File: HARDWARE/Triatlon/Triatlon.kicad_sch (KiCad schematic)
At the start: 18 parts, among them J1 TCRT5000-1, J2 TCRT5000-2, J3 Conn_01x10, J4 TCRT5000-3, J5 TB_1X2, SW1 SW1, U1 ESP32_DEVKITC, U2 Mini360, U3 AMS1117-3.3

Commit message: Prueba
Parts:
- added D1: 1N4148WT, Diode_SMD:D_SOD-523, symbol Diode:1N4148WT
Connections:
- net GND: now also U1.32 (GND), U1.38 (GND)
- net LPWM1: now also U1.23 (IO15)
- net LPWM2: now also U1.36 (IO22)
- net RPWM1: now also U1.26 (IO4)
- net RPWM2: now also U1.37 (IO23)
- net VCC: no longer J5.1
- new net: D1.1 (K), D1.2 (A)
- new net 7.4V: J5.1
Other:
- moved on the sheet: U1

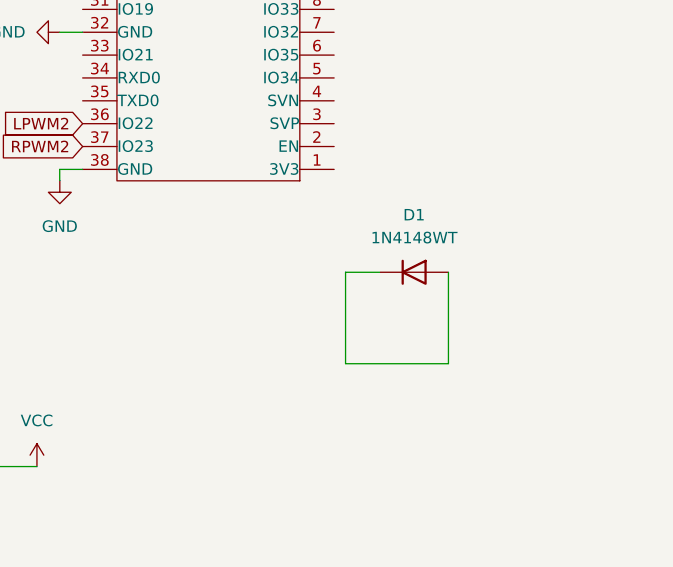
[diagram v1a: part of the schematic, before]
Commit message: Reestablezco el esquematico
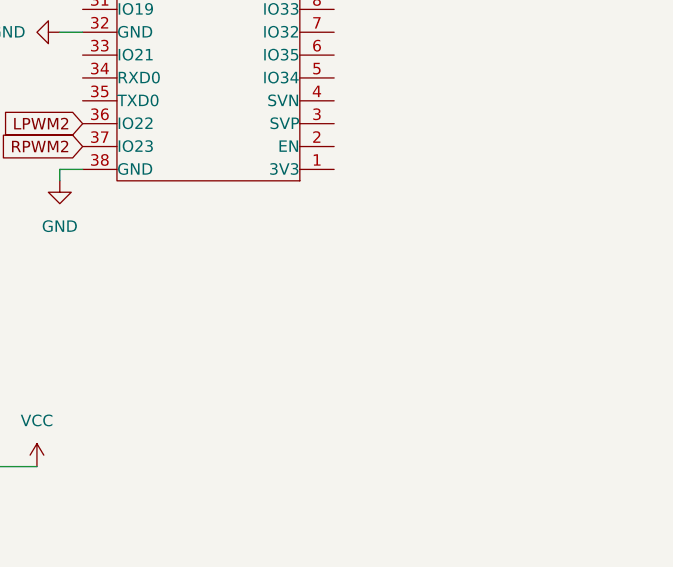
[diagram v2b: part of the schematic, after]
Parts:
- removed D1: 1N4148WT, Diode_SMD:D_SOD-523, symbol Diode:1N4148WT
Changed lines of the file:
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@@
 	(wire
 		(pts
-			(xy 127 121.92) (xy 127 111.76)
-		)
-		(stroke
-			(width 0)
-			(type default)
-		)
-	)
-	(wire
-		(pts
 			(xy 45.72 97.79) (xy 50.8 97.79)
 		)
@@
 	(wire
 		(pts
-			(xy 115.57 121.92) (xy 127 121.92)
-		)
-		(stroke
-			(width 0)
-			(type default)
-		)
-	)
-	(wire
-		(pts
 			(xy 50.8 97.79) (xy 55.88 97.79)
 		)
@@
 	(wire
 		(pts
-			(xy 115.57 111.76) (xy 115.57 121.92)
-		)
-		(stroke
-			(width 0)
-			(type default)
-		)
-	)
-	(wire
-		(pts
 			(xy 71.12 38.1) (xy 73.66 38.1)
 		)
@@
 	(wire
 		(pts
-			(xy 119.38 111.76) (xy 115.57 111.76)
-		)
-		(stroke
-			(width 0)
-			(type default)
-		)
-	)
-	(wire
-		(pts
 			(xy 140.97 31.75) (xy 143.51 31.75)
 		)
@@
 					(unit 1)
 				)
-			)
-		)
-	)
-	(symbol
-		(lib_id "Diode:1N4148WT")
-		(at 123.19 111.76 0)
-		(unit 1)
-		(exclude_from_sim no)
-		(in_bom yes)
-		(on_board yes)
-		(dnp no)
-		(fields_autoplaced yes)
-		(property "Reference" "D1"
-			(at 123.19 105.41 0)
-			(effects
-				(font
-					(size 1.27 1.27)
-				)
-			)
-		)
-		(property "Value" "1N4148WT"
-			(at 123.19 107.95 0)
-			(effects
-				(font
-					(size 1.27 1.27)
-				)
-			)
-		)
-		(property "Footprint" "Diode_SMD:D_SOD-523"
-			(at 123.19 116.205 0)
-			(effects
-				(font
-					(size 1.27 1.27)
-				)
-				(hide yes)
-			)
-		)
-		(property "Datasheet" "https://www.diodes.com/assets/Datasheets/ds30396.pdf"
-			(at 123.19 111.76 0)
-			(effects
-				(font
-					(size 1.27 1.27)
-				)
-				(hide yes)
-			)
-		)
-		(property "Description" "75V 0.15A Fast switching Diode, SOD-523"
-			(at 123.19 111.76 0)
-			(effects
-				(font
-					(size 1.27 1.27)
-				)
-				(hide yes)
-			)
-		)
-		(property "Sim.Device" "D"
-			(at 123.19 111.76 0)
-			(effects
-				(font
-					(size 1.27 1.27)
-				)
-				(hide yes)
-			)
-		)
-		(property "Sim.Pins" "1=K 2=A"
-			(at 123.19 111.76 0)
-			(effects
-				(font
-					(size 1.27 1.27)
-				)
-				(hide yes)
-			)
-		)
-		(pin "1"
-		)
-		(pin "2"
-		)
-		(instances
-			(project ""
-				(path "/d5286d43-c99d-4180-b950-0ade1916cf03"
-					(reference "D1")
-					(unit 1)
-				)
